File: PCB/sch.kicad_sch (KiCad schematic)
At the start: 0 parts

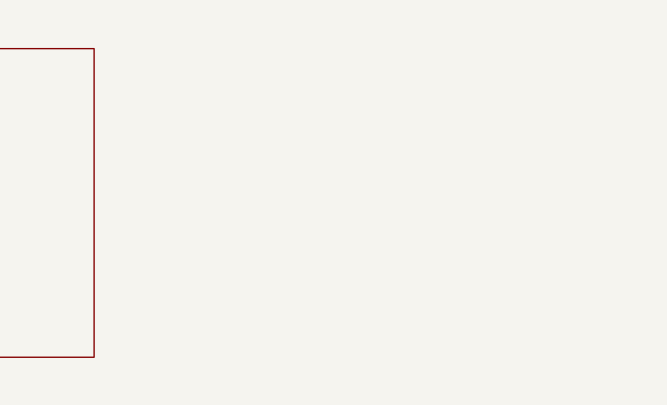
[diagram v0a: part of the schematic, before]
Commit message: broken 386 symbol
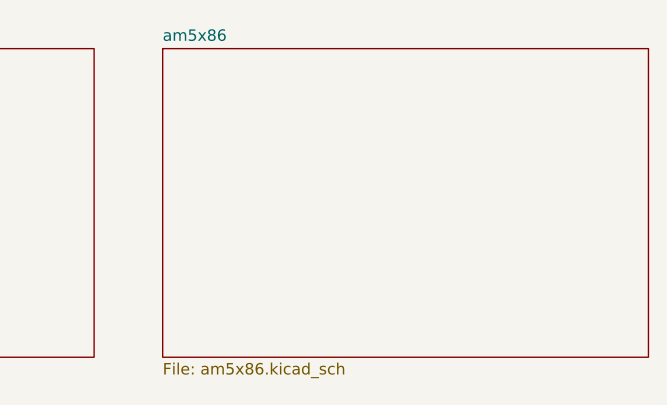
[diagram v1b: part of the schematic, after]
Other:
- added sheet am5x86 (am5x86.kicad_sch)
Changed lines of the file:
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@@
 	(paper "A4")
+	(sheet
+		(at 106.045 19.05)
+		(size 53.975 34.29)
+		(exclude_from_sim no)
+		(in_bom yes)
+		(on_board yes)
+		(dnp no)
+		(fields_autoplaced yes)
+		(stroke
+			(width 0.1524)
+			(type solid)
+		)
+		(fill
+			(color 0 0 0 0)
+		)
+		(property "Sheetname" "am5x86"
+			(at 106.045 18.3384 0)
+			(show_name no)
+			(do_not_autoplace no)
+			(effects
+				(font
+					(size 1.27 1.27)
+				)
+				(justify left bottom)
+			)
+		)
+		(property "Sheetfile" "am5x86.kicad_sch"
+			(at 106.045 53.9246 0)
+			(show_name no)
+			(do_not_autoplace no)
+			(effects
+				(font
+					(size 1.27 1.27)
+				)
+				(justify left top)
+			)
+		)
+		(instances
+			(project "Poor86"
+				(path "/516eb290-d08d-4e43-95ba-5c21610df4ad"
+					(page "4")
+				)
+			)
+		)
+	)
 	(sheet
 		(at 62.23 19.05)

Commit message: progress
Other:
- removed sheet 386486SX
- added sheet A_PGND (AsicPowerGnd.kicad_sch)
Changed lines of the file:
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@@
 	(paper "A4")
 	(sheet
-		(at 106.045 19.05)
+		(at 20.32 19.685)
+		(size 42.545 56.515)
+		(exclude_from_sim no)
+		(in_bom yes)
+		(on_board yes)
+		(dnp no)
+		(fields_autoplaced yes)
+		(stroke
+			(width 0.1524)
+			(type solid)
+		)
+		(fill
+			(color 0 0 0 0)
+		)
+		(property "Sheetname" "A_PGND"
+			(at 20.32 18.9734 0)
+			(show_name no)
+			(do_not_autoplace no)
+			(effects
+				(font
+					(size 1.27 1.27)
+				)
+				(justify left bottom)
+			)
+		)
+		(property "Sheetfile" "AsicPowerGnd.kicad_sch"
+			(at 20.32 76.7846 0)
+			(show_name no)
+			(do_not_autoplace no)
+			(effects
+				(font
+					(size 1.27 1.27)
+				)
+				(justify left top)
+			)
+		)
+		(instances
+			(project "Poor86"
+				(path "/516eb290-d08d-4e43-95ba-5c21610df4ad"
+					(page "3")
+				)
+			)
+		)
+	)
+	(sheet
+		(at 187.96 26.67)
 		(size 53.975 34.29)
 		(exclude_from_sim no)
@@
 		)
 		(property "Sheetname" "am5x86"
-			(at 106.045 18.3384 0)
+			(at 187.96 25.9584 0)
 			(show_name no)
 			(do_not_autoplace no)
@@
 		)
 		(property "Sheetfile" "am5x86.kicad_sch"
-			(at 106.045 53.9246 0)
+			(at 187.96 61.5446 0)
 			(show_name no)
 			(do_not_autoplace no)
@@
 	)
 	(sheet
-		(at 62.23 19.05)
-		(size 36.195 34.29)
-		(exclude_from_sim no)
-		(in_bom yes)
-		(on_board yes)
-		(dnp no)
-		(fields_autoplaced yes)
-		(stroke
-			(width 0.1524)
-			(type solid)
-		)
-		(fill
-			(color 0 0 0 0)
-		)
-		(property "Sheetname" "386486SX"
-			(at 62.23 18.3384 0)
-			(show_name no)
-			(do_not_autoplace no)
-			(effects
-				(font
-					(size 1.27 1.27)
-				)
-				(justify left bottom)
-			)
-		)
-		(property "Sheetfile" "x86SX.kicad_sch"
-			(at 62.23 53.9246 0)
-			(show_name no)
-			(do_not_autoplace no)
-			(effects
-				(font
-					(size 1.27 1.27)
-				)
-				(justify left top)
-			)
-		)
-		(instances
-			(project "Poor86"
-				(path "/516eb290-d08d-4e43-95ba-5c21610df4ad"
-					(page "3")
-				)
-			)
-		)
-	)
-	(sheet
-		(at 16.51 18.415)
+		(at 192.405 76.835)
 		(size 40.005 35.56)
 		(exclude_from_sim no)
@@
 		)
 		(property "Sheetname" "FPGA"
-			(at 16.51 17.7034 0)
+			(at 192.405 76.1234 0)
 			(show_name no)
 			(do_not_autoplace no)
@@
 		)
 		(property "Sheetfile" "FPGA.kicad_sch"
-			(at 16.51 54.5596 0)
+			(at 192.405 112.9796 0)
 			(show_name no)
 			(do_not_autoplace no)

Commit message: more progress
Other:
- added sheet Memory (mems.kicad_sch)
- added sheet eternal_perif (external_perif.kicad_sch)
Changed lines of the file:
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@@
 	)
 	(sheet
-		(at 187.96 26.67)
+		(at 222.25 20.32)
 		(size 53.975 34.29)
 		(exclude_from_sim no)
@@
 		)
 		(property "Sheetname" "am5x86"
-			(at 187.96 25.9584 0)
+			(at 222.25 19.6084 0)
 			(show_name no)
 			(do_not_autoplace no)
@@
 		)
 		(property "Sheetfile" "am5x86.kicad_sch"
-			(at 187.96 61.5446 0)
+			(at 222.25 55.1946 0)
 			(show_name no)
 			(do_not_autoplace no)
@@
 	)
 	(sheet
-		(at 192.405 76.835)
+		(at 80.01 22.225)
+		(size 86.995 56.515)
+		(exclude_from_sim no)
+		(in_bom yes)
+		(on_board yes)
+		(dnp no)
+		(fields_autoplaced yes)
+		(stroke
+			(width 0.1524)
+			(type solid)
+		)
+		(fill
+			(color 0 0 0 0)
+		)
+		(property "Sheetname" "Memory"
+			(at 80.01 21.5134 0)
+			(show_name no)
+			(do_not_autoplace no)
+			(effects
+				(font
+					(size 1.27 1.27)
+				)
+				(justify left bottom)
+			)
+		)
+		(property "Sheetfile" "mems.kicad_sch"
+			(at 80.01 79.3246 0)
+			(show_name no)
+			(do_not_autoplace no)
+			(effects
+				(font
+					(size 1.27 1.27)
+				)
+				(justify left top)
+			)
+		)
+		(instances
+			(project "Poor86"
+				(path "/516eb290-d08d-4e43-95ba-5c21610df4ad"
+					(page "5")
+				)
+			)
+		)
+	)
+	(sheet
+		(at 81.915 94.615)
+		(size 90.805 54.61)
+		(exclude_from_sim no)
+		(in_bom yes)
+		(on_board yes)
+		(dnp no)
+		(fields_autoplaced yes)
+		(stroke
+			(width 0.1524)
+			(type solid)
+		)
+		(fill
+			(color 0 0 0 0)
+		)
+		(property "Sheetname" "eternal_perif"
+			(at 81.915 93.9034 0)
+			(show_name no)
+			(do_not_autoplace no)
+			(effects
+				(font
+					(size 1.27 1.27)
+				)
+				(justify left bottom)
+			)
+		)
+		(property "Sheetfile" "external_perif.kicad_sch"
+			(at 81.915 149.8096 0)
+			(show_name no)
+			(do_not_autoplace no)
+			(effects
+				(font
+					(size 1.27 1.27)
+				)
+				(justify left top)
+			)
+		)
+		(instances
+			(project "Poor86"
+				(path "/516eb290-d08d-4e43-95ba-5c21610df4ad"
+					(page "6")
+				)
+			)
+		)
+	)
+	(sheet
+		(at 235.585 61.595)
 		(size 40.005 35.56)
 		(exclude_from_sim no)
@@
 		)
 		(property "Sheetname" "FPGA"
-			(at 192.405 76.1234 0)
+			(at 235.585 60.8834 0)
 			(show_name no)
 			(do_not_autoplace no)
@@
 		)
 		(property "Sheetfile" "FPGA.kicad_sch"
-			(at 192.405 112.9796 0)
+			(at 235.585 97.7396 0)
 			(show_name no)
 			(do_not_autoplace no)

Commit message: more progress
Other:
- added sheet VideoSubSystem (video.kicad_sch)
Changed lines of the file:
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@@
 	)
 	(sheet
-		(at 81.915 94.615)
+		(at 133.35 98.425)
 		(size 90.805 54.61)
 		(exclude_from_sim no)
@@
 		)
 		(property "Sheetname" "eternal_perif"
-			(at 81.915 93.9034 0)
+			(at 133.35 97.7134 0)
 			(show_name no)
 			(do_not_autoplace no)
@@
 		)
 		(property "Sheetfile" "external_perif.kicad_sch"
-			(at 81.915 149.8096 0)
+			(at 133.35 153.6196 0)
 			(show_name no)
 			(do_not_autoplace no)
@@
 				)
 			)
+		)
+	)
+	(sheet
+		(at 26.035 94.615)
+		(size 86.36 69.85)
+		(exclude_from_sim no)
+		(in_bom yes)
+		(on_board yes)
+		(dnp no)
+		(fields_autoplaced yes)
+		(stroke
+			(width 0.1524)
+			(type solid)
+		)
+		(fill
+			(color 0 0 0 0)
+		)
+		(property "Sheetname" "VideoSubSystem"
+			(at 26.035 93.9034 0)
+			(show_name no)
+			(do_not_autoplace no)
+			(effects
+				(font
+					(size 1.27 1.27)
+				)
+				(justify left bottom)
+			)
+		)
+		(property "Sheetfile" "video.kicad_sch"
+			(at 26.035 165.0496 0)
+			(show_name no)
+			(do_not_autoplace no)
+			(effects
+				(font
+					(size 1.27 1.27)
+				)
+				(justify left top)
+			)
+		)
+		(property "Field2" ""
+			(at 26.035 94.615 0)
+			(hide yes)
+			(show_name no)
+			(do_not_autoplace no)
+			(effects
+				(font
+					(size 1.27 1.27)
+				)
+			)
+		)
+		(instances
+			(project "Poor86"
+				(path "/516eb290-d08d-4e43-95ba-5c21610df4ad"
+					(page "7")
+				)
+			)

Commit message: route-out in progress
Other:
- added sheet Untitled Sheet (untitled.kicad_sch)
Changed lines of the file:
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@@
 	)
 	(sheet
-		(at 133.35 98.425)
+		(at 191.135 107.315)
 		(size 90.805 54.61)
 		(exclude_from_sim no)
@@
 		)
 		(property "Sheetname" "eternal_perif"
-			(at 133.35 97.7134 0)
+			(at 191.135 106.6034 0)
 			(show_name no)
 			(do_not_autoplace no)
@@
 		)
 		(property "Sheetfile" "external_perif.kicad_sch"
-			(at 133.35 153.6196 0)
+			(at 191.135 162.5096 0)
 			(show_name no)
 			(do_not_autoplace no)
@@
 				)
 			)
+		)
+	)
+	(sheet
+		(at 116.205 94.615)
+		(size 73.025 66.675)
+		(exclude_from_sim no)
+		(in_bom yes)
+		(on_board yes)
+		(dnp no)
+		(fields_autoplaced yes)
+		(stroke
+			(width 0.1524)
+			(type solid)
+		)
+		(fill
+			(color 0 0 0 0)
+		)
+		(property "Sheetname" "Untitled Sheet"
+			(at 116.205 93.9034 0)
+			(show_name no)
+			(do_not_autoplace no)
+			(effects
+				(font
+					(size 1.27 1.27)
+				)
+				(justify left bottom)
+			)
+		)
+		(property "Sheetfile" "untitled.kicad_sch"
+			(at 116.205 161.8746 0)
+			(show_name no)
+			(do_not_autoplace no)
+			(effects
+				(font
+					(size 1.27 1.27)
+				)
+				(justify left top)
+			)
+		)
+		(instances
+			(project "Poor86"
+				(path "/516eb290-d08d-4e43-95ba-5c21610df4ad"
+					(page "8")
+				)
+			)
